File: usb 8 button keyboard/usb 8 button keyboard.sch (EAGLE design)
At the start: 28 parts, among them Q1 MMBT2222A, U1 ATMEGA32U4-AU, Y1 16MHZ

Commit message: new version. 9 buttons!
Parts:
- added R11: 100, cheeper:R-US_R0402
- added U$15: CHERRY-MX-LED, cherrymx:CHERRY-MX-LED
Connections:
- new net N$4: R11.1, U$15.LED1
- new net SW8: U$15.SW1, U1.PC7(ICP3/CLK0/OC4A)
- net BL: now also R11.2
- net GND: now also U$15.LED2, U$15.SW2
- net PLED: now also U1.PF7(ADC7(TDI); no longer U1.PD5(XCK/CTS)
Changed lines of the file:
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@@
 <part name="R10" library="cheeper" deviceset="R-US_" device="R0402" value="100"/>
 <part name="SUPPLY5" library="cheeper" deviceset="VCC5V" device=""/>
+<part name="U$15" library="cherrymx" deviceset="CHERRY-MX-LED" device=""/>
+<part name="R11" library="cheeper" deviceset="R-US_" device="R0402" value="100"/>
 </parts>
 <sheets>
@@
 <instance part="R10" gate="G$1" x="144.78" y="91.44" rot="R90"/>
 <instance part="SUPPLY5" gate="+5V" x="144.78" y="111.76"/>
+<instance part="U$15" gate="G$1" x="403.86" y="66.04"/>
+<instance part="R11" gate="G$1" x="424.18" y="76.2" rot="R90"/>
 </instances>
 <busses>
@@
 <junction x="381" y="86.36"/>
 <pinref part="U$14" gate="M" pin="GND"/>
+<pinref part="U$15" gate="G$1" pin="SW2"/>
+<wire x1="393.7" y1="63.5" x2="391.16" y2="63.5" width="0.1524" layer="91"/>
+<wire x1="391.16" y1="63.5" x2="391.16" y2="55.88" width="0.1524" layer="91"/>
+<wire x1="391.16" y1="55.88" x2="388.62" y2="55.88" width="0.1524" layer="91"/>
+<pinref part="U$15" gate="G$1" pin="LED2"/>
+<wire x1="421.64" y1="63.5" x2="424.18" y2="63.5" width="0.1524" layer="91"/>
+<wire x1="424.18" y1="63.5" x2="424.18" y2="55.88" width="0.1524" layer="91"/>
+<wire x1="424.18" y1="55.88" x2="391.16" y2="55.88" width="0.1524" layer="91"/>
+<junction x="391.16" y="55.88"/>
 </segment>
 </net>
@@
 <junction x="248.92" y="111.76"/>
 <junction x="246.38" y="111.76"/>
+<wire x1="424.18" y1="111.76" x2="383.54" y2="111.76" width="0.1524" layer="91"/>
+<junction x="383.54" y="111.76"/>
+<pinref part="R11" gate="G$1" pin="2"/>
+<wire x1="424.18" y1="81.28" x2="424.18" y2="111.76" width="0.1524" layer="91"/>
 </segment>
 </net>
 <net name="PLED" class="0">
-<segment>
-<pinref part="U1" gate="G$1" pin="PD5(XCK/CTS)"/>
-<wire x1="132.08" y1="127" x2="142.24" y2="127" width="0.1524" layer="91"/>
-<label x="139.7" y="127" size="1.778" layer="95"/>
-</segment>
 <segment>
 <wire x1="144.78" y1="83.82" x2="152.4" y2="83.82" width="0.1524" layer="91"/>
@@
 <label x="149.86" y="83.82" size="1.778" layer="95"/>
 </segment>
+<segment>
+<pinref part="U1" gate="G$1" pin="PF7(ADC7(TDI)"/>
+<wire x1="132.08" y1="175.26" x2="144.78" y2="175.26" width="0.1524" layer="91"/>
+<label x="139.7" y="175.26" size="1.778" layer="95"/>
+</segment>
 </net>
 <net name="N$3" class="0">
@@
 </segment>
 </net>
+<net name="N$4" class="0">
+<segment>
+<pinref part="U$15" gate="G$1" pin="LED1"/>
+<wire x1="421.64" y1="68.58" x2="424.18" y2="68.58" width="0.1524" layer="91"/>
+<pinref part="R11" gate="G$1" pin="1"/>
+<wire x1="424.18" y1="68.58" x2="424.18" y2="71.12" width="0.1524" layer="91"/>
+</segment>
+</net>
+<net name="SW8" class="0">
+<segment>
+<pinref part="U$15" gate="G$1" pin="SW1"/>
+<wire x1="393.7" y1="68.58" x2="391.16" y2="68.58" width="0.1524" layer="91"/>
+<wire x1="391.16" y1="68.58" x2="391.16" y2="73.66" width="0.1524" layer="91"/>
+<wire x1="391.16" y1="73.66" x2="401.32" y2="73.66" width="0.1524" layer="91"/>
+<label x="396.24" y="73.66" size="1.778" layer="95"/>
+</segment>
+<segment>
+<pinref part="U1" gate="G$1" pin="PC7(ICP3/CLK0/OC4A)"/>
+<wire x1="132.08" y1="160.02" x2="144.78" y2="160.02" width="0.1524" layer="91"/>
+<label x="139.7" y="160.02" size="1.778" layer="95"/>
+</segment>
+</net>

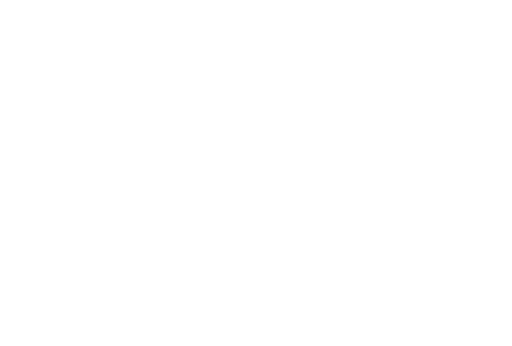
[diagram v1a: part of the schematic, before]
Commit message: cleaned up silk, rotated mx switches so LED's are on top, cleaned up some redundent ass routing. added ROHS cert logo.
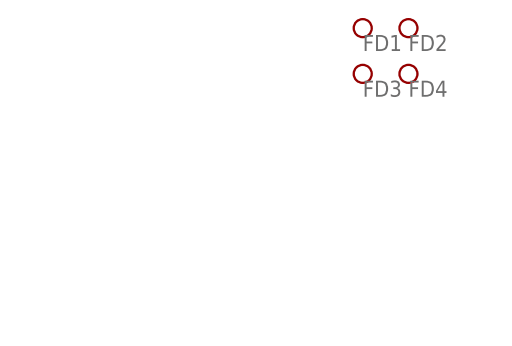
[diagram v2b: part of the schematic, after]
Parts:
- added FD1, FD2, FD3, FD4: FIDUCIAL, ChipTestJig:FIDUCIAL
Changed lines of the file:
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@@
 <part name="U$15" library="cherrymx" deviceset="CHERRY-MX-LED" device=""/>
 <part name="R11" library="cheeper" deviceset="R-US_" device="R0402" value="100"/>
+<part name="FD1" library="ChipTestJig" deviceset="FIDUCIAL" device=""/>
+<part name="FD2" library="ChipTestJig" deviceset="FIDUCIAL" device=""/>
+<part name="FD3" library="ChipTestJig" deviceset="FIDUCIAL" device=""/>
+<part name="FD4" library="ChipTestJig" deviceset="FIDUCIAL" device=""/>
 </parts>
 <sheets>
@@
 <instance part="U$15" gate="G$1" x="403.86" y="66.04"/>
 <instance part="R11" gate="G$1" x="424.18" y="76.2" rot="R90"/>
+<instance part="FD1" gate="G$1" x="414.02" y="271.78"/>
+<instance part="FD2" gate="G$1" x="419.1" y="271.78"/>
+<instance part="FD3" gate="G$1" x="414.02" y="266.7"/>
+<instance part="FD4" gate="G$1" x="419.1" y="266.7"/>
 </instances>
 <busses>
